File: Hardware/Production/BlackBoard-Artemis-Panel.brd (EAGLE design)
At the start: 167.6 x 120.9 mm, 522 parts, among them IC1 LM1117, IC2 LM1117, IC3 LM1117, IC4 LM1117, J10 CORTEX_DEBUG, J13 POWER_JACKTOE, J15 USB-C, J16 CORTEX_DEBUG, J19 POWER_JACKTOE, J2 CORTEX_DEBUG, J21 USB-C, J22 CORTEX_DEBUG, J3 POWER_JACKTOE, J5 USB-C, J6 POWER_JACKTOE, J9 USB-C, Q1 1.1A/60V/600mΩ, Q2 1.1A/60V/600mΩ, Q3 1.1A/60V/600mΩ, Q4 1.1A/60V/600mΩ, U1 AP2112-3.3V, U10 AP2112-3.3V, U11 CH340C, U12 ARTEMIS_MODULESMD, U2 CH340C, U3 AP2112-3.3V, U4 ARTEMIS_MODULESMD, U5 CH340C, U6 ARTEMIS_MODULESMD, U7 AP2112-3.3V, U8 CH340C, U9 ARTEMIS_MODULESMD, Y1 32.768kHz, Y2 32.768kHz, Y3 32.768kHz, Y4 32.768kHz

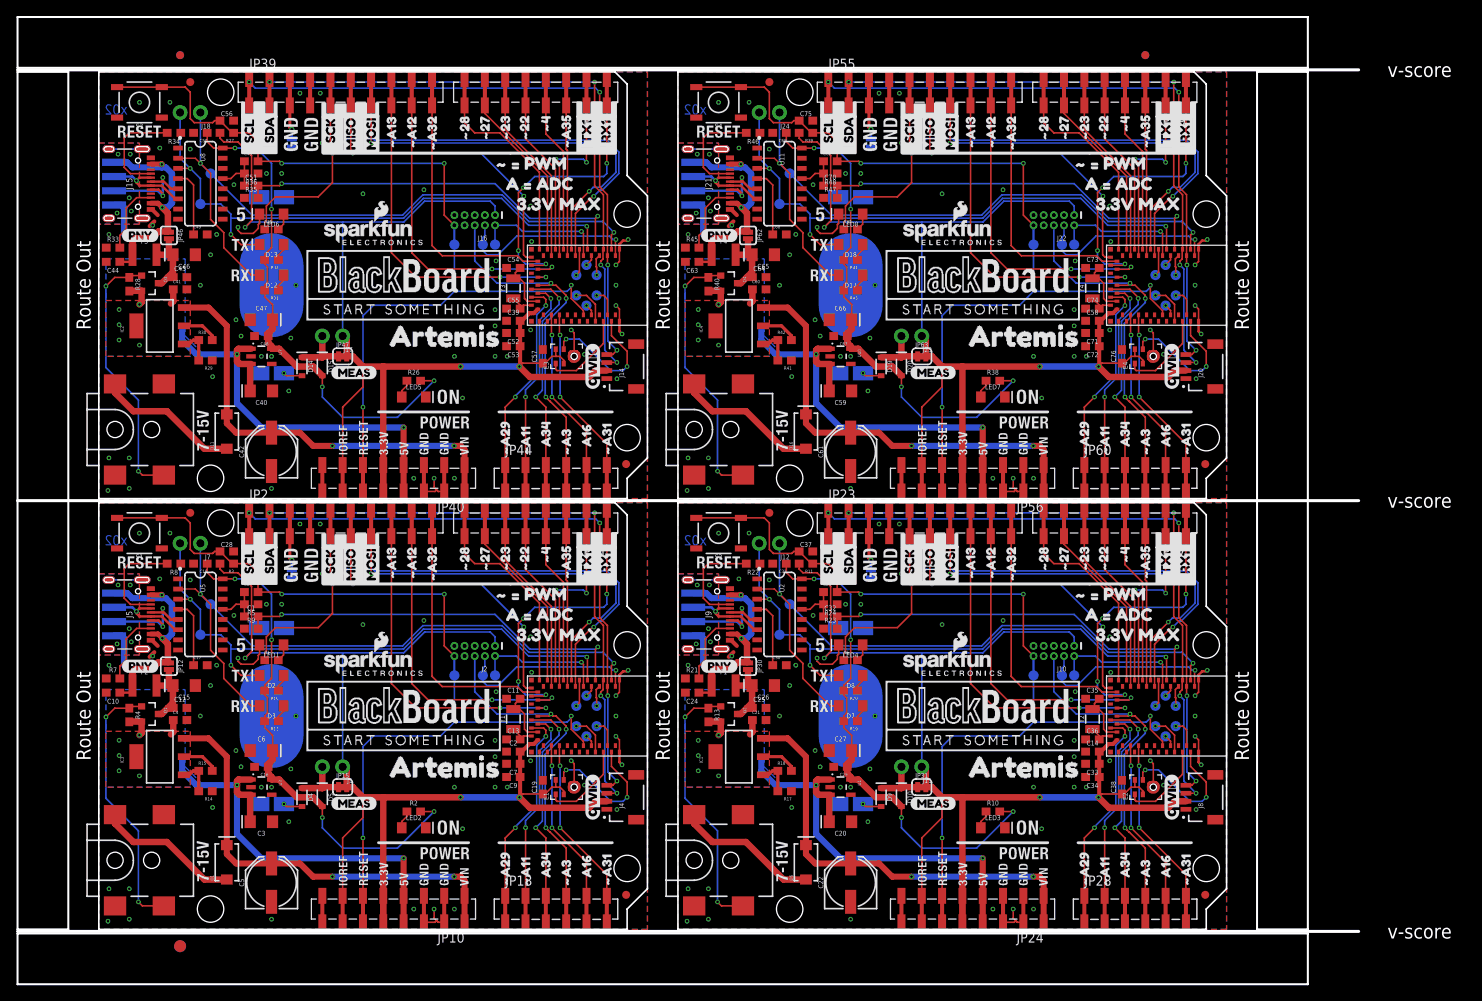
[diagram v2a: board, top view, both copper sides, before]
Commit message: Adding ignore. Adding production panel.
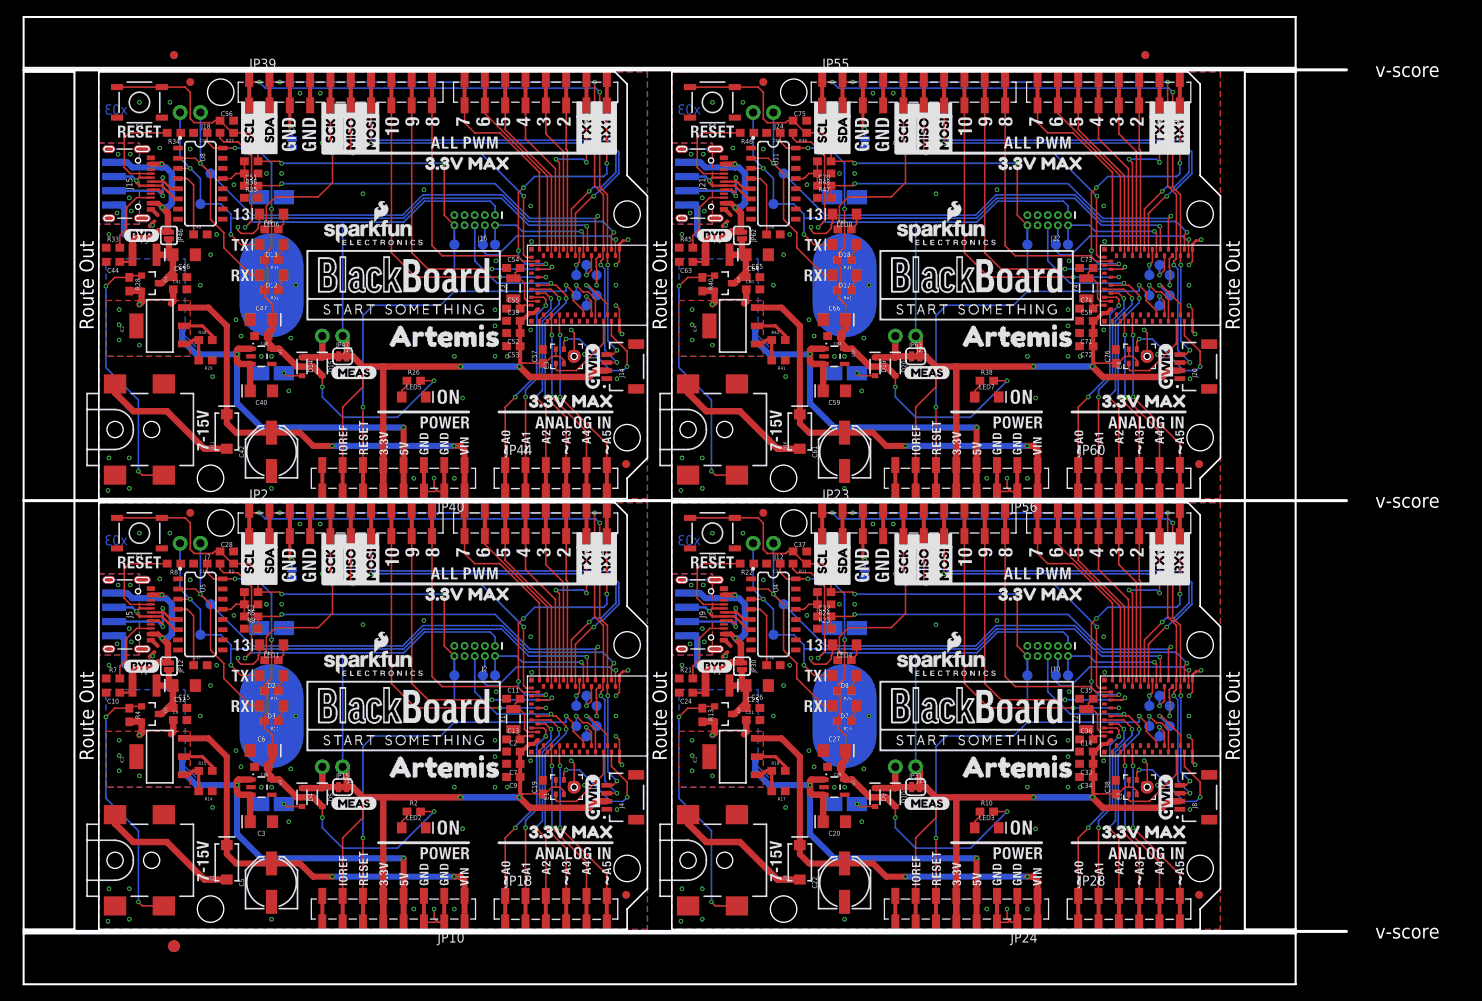
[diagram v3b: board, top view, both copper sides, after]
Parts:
- removed U$125, U$172: (no value), buzzard_labels (1):#425
- removed U$126, U$173: (no value), buzzard_labels (1):#434
- removed U$127, U$174: (no value), buzzard_labels (1):80
- removed U$128, U$175: (no value), buzzard_labels (1):91
- removed U$129, U$176: (no value), buzzard_labels (1):102
- removed U$130, U$177: (no value), buzzard_labels (1):383
- removed U$131, U$178: (no value), buzzard_labels (2):#_#_PWM7
- removed U$132, U$179: (no value), buzzard_labels (2):3#3V_MAX2
- removed U$133, U$180: (no value), buzzard_labels (2):A_#_ADC6
- removed U$134, U$181: (no value), buzzard_labels (2):MEAS3
- removed U$135, U$182: (no value), buzzard_labels (2):RX11
- removed U$136, U$183: (no value), buzzard_labels (2):TX10
- removed U$137, U$184: (no value), buzzard_labels (3):RX01
- removed U$138, U$185: (no value), buzzard_labels (3):TX00
- removed U$139, U$186: (no value), buzzard_labels (5):AREF2
- removed U$140, U$187: (no value), buzzard_labels (6):SCL1
- removed U$141, U$188: (no value), buzzard_labels (6):SDA0
- removed U$142: OSHW-LOGOS, SparkFun-Aesthetics:OSHW-LOGO-S
- removed U$143, U$144: (no value), blackboardlogo:BLACKBOARDLOGO#PNG
- removed U$145: (no value), madeinusa:MADEINUSA#PNG
- removed U$146: (no value), Labels:QWIIC_COPYRIGHT_SMALL
- removed U$147: (no value), buzzard_labels (13):G1
- removed U$148: (no value), buzzard_labels (13):V0
- removed U$149: (no value), buzzard_labels (14):D#3
- removed U$150: (no value), buzzard_labels (14):D#4
- removed U$151: (no value), buzzard_labels:PNY0
- removed U$152, U$153: (no value), buzzard_labels (3):ARTEMIS0
- removed U$154: (no value), buzzard_labels:A160
- removed U$155: (no value), buzzard_labels (1):#48
- removed U$156: (no value), buzzard_labels (1):#229
- removed U$157: (no value), buzzard_labels (1):#2310
- removed U$158: (no value), buzzard_labels (1):#2711
- removed U$159: (no value), buzzard_labels (1):#2812
- removed U$160: (no value), buzzard_labels (1):#A31
- removed U$161: (no value), buzzard_labels (1):#A113
- removed U$162: (no value), buzzard_labels (1):#A294
- removed U$163: (no value), buzzard_labels (1):#A310
- removed U$164: (no value), buzzard_labels (1):#A357
- removed U$165: (no value), buzzard_labels (1):#A1214
- removed U$166: (no value), buzzard_labels (1):#A1315
- removed U$167: (no value), buzzard_labels (1):#A3213
- removed U$168: (no value), buzzard_labels (1):A342
- removed U$169: (no value), buzzard_labels (8):MISO8
- removed U$170: (no value), buzzard_labels (8):MOSI7
- removed U$171: (no value), buzzard_labels (8):SCK9
- U$100: device buzzard_labels (13):G1 -> buzzard_labels (13):V0
- U$101: device buzzard_labels (13):V0 -> buzzard_labels (14):D#3
- U$102: device buzzard_labels (14):D#3 -> buzzard_labels (14):D#4
- U$103: device buzzard_labels (14):D#4 -> buzzard_labels (3):ARTEMIS0
- U$104: device buzzard_labels:PNY0 -> buzzard_labels (3):ARTEMIS0
- U$105: device buzzard_labels (3):ARTEMIS0 -> buzzard_labels (8):MISO8
- U$106: device buzzard_labels (3):ARTEMIS0 -> buzzard_labels (8):MOSI7
- U$107: device buzzard_labels:A160 -> buzzard_labels (8):SCK9
- U$108: device buzzard_labels (1):#48 -> buzzard_labels (2):3#3V_MAX2
- U$109: device buzzard_labels (1):#229 -> buzzard_labels (2):MEAS3
- U$110: device buzzard_labels (1):#2310 -> buzzard_labels (2):RX11
- U$111: device buzzard_labels (1):#2711 -> buzzard_labels (2):TX10
- U$112: device buzzard_labels (1):#2812 -> buzzard_labels (3):RX01
- U$113: device buzzard_labels (1):#A31 -> buzzard_labels (3):TX00
- U$114: device buzzard_labels (1):#A113 -> buzzard_labels (5):AREF2
- U$115: device buzzard_labels (1):#A294 -> buzzard_labels (6):SCL1
- U$116: device buzzard_labels (1):#A310 -> buzzard_labels (6):SDA0
- U$117: device buzzard_labels (1):#A357 -> buzzard_labels (13):BYP0
- U$118: device buzzard_labels (1):#A1214 -> buzzard_labels (2):3#3V_MAX2
- U$119: device buzzard_labels (1):#A1315 -> buzzard_labels (2):#284
- U$120: device buzzard_labels (1):#A3213 -> buzzard_labels (2):#295
- U$121: device buzzard_labels (1):A342 -> buzzard_labels (2):240
- U$122: device buzzard_labels (8):MISO8 -> buzzard_labels (2):251
- U$123: device buzzard_labels (8):MOSI7 -> buzzard_labels (2):262
- U$124: device buzzard_labels (8):SCK9 -> buzzard_labels (2):273
- U$13: device buzzard_labels:PNY0 -> buzzard_labels (2):3#3V_MAX2
- U$17: device buzzard_labels:A160 -> buzzard_labels (2):#284
- U$19: device buzzard_labels (1):#48 -> buzzard_labels (2):#295
- U$21: device buzzard_labels (1):#229 -> buzzard_labels (2):240
- U$23: device Labels:QWIIC_COPYRIGHT_SMALL -> buzzard_labels (2):251
- U$24: device buzzard_labels (13):G1 -> buzzard_labels (2):262
- U$25: device buzzard_labels (1):#2310 -> buzzard_labels (2):273
- U$26: device buzzard_labels (1):#2711 -> Labels:QWIIC_COPYRIGHT_SMALL
- U$27: device buzzard_labels (1):#2812 -> buzzard_labels (13):G1
- U$28: device buzzard_labels (1):#A31 -> buzzard_labels (13):V0
- U$29: device buzzard_labels (1):#A113 -> buzzard_labels (14):D#3
- U$30: device buzzard_labels (1):#A294 -> buzzard_labels (14):D#4
- U$31: device buzzard_labels (1):#A310 -> buzzard_labels (3):ARTEMIS0
- U$32: device buzzard_labels (13):V0 -> buzzard_labels (3):ARTEMIS0
- U$33: device buzzard_labels (1):#A357 -> buzzard_labels (8):MISO8
- U$34: device buzzard_labels (1):#A1214 -> buzzard_labels (8):MOSI7
- U$35: device buzzard_labels (1):#A1315 -> buzzard_labels (8):SCK9
- U$36: device buzzard_labels (1):#A3213 -> buzzard_labels (2):3#3V_MAX2
- U$37: device buzzard_labels (14):D#3 -> buzzard_labels (2):MEAS3
- U$38: device buzzard_labels (1):A342 -> buzzard_labels (2):RX11
- U$39: device buzzard_labels (14):D#4 -> buzzard_labels (2):TX10
- U$40: device buzzard_labels:PNY0 -> buzzard_labels (3):RX01
- U$41: device buzzard_labels (3):ARTEMIS0 -> buzzard_labels (3):TX00
- U$42: device buzzard_labels (3):ARTEMIS0 -> buzzard_labels (5):AREF2
- U$43: device buzzard_labels:A160 -> buzzard_labels (6):SCL1
- U$44: device buzzard_labels (1):#48 -> buzzard_labels (6):SDA0
- U$45: device buzzard_labels (1):#229 -> buzzard_labels (13):BYP0
- U$46: device buzzard_labels (1):#2310 -> buzzard_labels (2):3#3V_MAX2
- U$51: device buzzard_labels (1):#2711 -> buzzard_labels (2):#284
- U$52: device buzzard_labels (1):#2812 -> buzzard_labels (2):#295
- U$54: device buzzard_labels (1):#A31 -> buzzard_labels (2):240
- U$55: device buzzard_labels (1):#A113 -> buzzard_labels (2):251
- U$56: device buzzard_labels (1):#A294 -> buzzard_labels (2):262
- U$57: device buzzard_labels (1):#A310 -> buzzard_labels (2):273
- U$58: value (none) -> OSHW-LOGOS; device buzzard_labels (1):#A357 -> SparkFun-Aesthetics:OSHW-LOGO-S
- U$59: device buzzard_labels (1):#A1214 -> blackboardlogo:BLACKBOARDLOGO#PNG
- U$60: device buzzard_labels (1):#425 -> blackboardlogo:BLACKBOARDLOGO#PNG
- U$61: device buzzard_labels (1):#434 -> madeinusa:MADEINUSA#PNG
- U$62: device buzzard_labels (1):80 -> Labels:QWIIC_COPYRIGHT_SMALL
- U$63: device buzzard_labels (1):91 -> buzzard_labels (13):G1
- U$64: device buzzard_labels (1):102 -> buzzard_labels (13):V0
- U$65: device buzzard_labels (1):383 -> buzzard_labels (14):D#3
- U$66: device buzzard_labels (2):#_#_PWM7 -> buzzard_labels (14):D#4
- U$68: device buzzard_labels (1):#A1315 -> buzzard_labels (13):BYP0
- U$69: device buzzard_labels (2):A_#_ADC6 -> buzzard_labels (3):ARTEMIS0
- U$73: device buzzard_labels (1):#A3213 -> buzzard_labels (3):ARTEMIS0
- U$74: device buzzard_labels (1):A342 -> buzzard_labels (8):MISO8
- U$75: device buzzard_labels (8):MISO8 -> buzzard_labels (8):MOSI7
- U$76: device buzzard_labels (8):MOSI7 -> buzzard_labels (8):SCK9
- U$77: device buzzard_labels (8):SCK9 -> buzzard_labels (2):3#3V_MAX2
- U$78: device buzzard_labels (1):#425 -> buzzard_labels (2):MEAS3
- U$79: device buzzard_labels (1):#434 -> buzzard_labels (2):RX11
- U$80: device buzzard_labels (1):80 -> buzzard_labels (2):TX10
- U$81: device buzzard_labels (1):91 -> buzzard_labels (3):RX01
- U$82: device buzzard_labels (1):102 -> buzzard_labels (3):TX00
- U$83: device buzzard_labels (1):383 -> buzzard_labels (5):AREF2
- U$84: device buzzard_labels (2):#_#_PWM7 -> buzzard_labels (6):SCL1
- U$85: device buzzard_labels (2):3#3V_MAX2 -> buzzard_labels (6):SDA0
- U$86: device buzzard_labels (2):A_#_ADC6 -> buzzard_labels (13):BYP0
- U$87: device buzzard_labels (2):MEAS3 -> buzzard_labels (2):3#3V_MAX2
- U$88: device buzzard_labels (2):RX11 -> buzzard_labels (2):#284
- U$89: device buzzard_labels (2):TX10 -> buzzard_labels (2):#295
- U$90: device buzzard_labels (3):RX01 -> buzzard_labels (2):240
- U$91: device buzzard_labels (3):TX00 -> buzzard_labels (2):251
- U$92: device buzzard_labels (5):AREF2 -> buzzard_labels (2):262
- U$93: device buzzard_labels (6):SCL1 -> buzzard_labels (2):273
- U$94: value (none) -> OSHW-LOGOS; device buzzard_labels (6):SDA0 -> SparkFun-Aesthetics:OSHW-LOGO-S
- U$95: value OSHW-LOGOS -> (none); device SparkFun-Aesthetics:OSHW-LOGO-S -> blackboardlogo:BLACKBOARDLOGO#PNG
- U$97: device blackboardlogo:BLACKBOARDLOGO#PNG -> madeinusa:MADEINUSA#PNG
- U$98: device madeinusa:MADEINUSA#PNG -> Labels:QWIIC_COPYRIGHT_SMALL
- U$99: device Labels:QWIIC_COPYRIGHT_SMALL -> buzzard_labels (13):G1
- U1: value AP2112-3.3V -> ARTEMIS_MODULESMD; device SparkFun-PowerIC:SOT23-5 -> Testing:ARTEMIS_FP
- U2: value CH340C -> AP2112-3.3V; device SparkFun-IC-Comms:SO016 -> SparkFun-PowerIC:SOT23-5
- U4: value ARTEMIS_MODULESMD -> CH340C; device Testing:ARTEMIS_FP -> SparkFun-IC-Comms:SO016
- moved U$81 142.6 mm to (12.7, 96.3), turned to 90 degrees
- moved U$58 142.6 mm to (2.54, 105.2), flipped to the bottom, turned to 0 degrees
- moved U$82 140.8 mm to (10.2, 96.3), turned to 90 degrees
- moved U$83 134.8 mm to (26.9, 100.6)
- moved U$74 132.8 mm to (31.5, 96.4)
- moved U$86 128.0 mm to (3.05, 86.7)
- moved U$104 124.1 mm to (126.7, 91.9), flipped to the bottom
- moved U$85 118.4 mm to (21.3, 97.3), turned to 90 degrees
- moved U$84 115.9 mm to (18.8, 97.3), turned to 90 degrees
- moved U$78 111.4 mm to (29.0, 69.6), flipped to the top
- moved U$124 110.7 mm to (138.2, 79.2), flipped to the bottom, turned to 0 degrees
- moved U$95 110.0 mm to (109.7, 80.5), flipped to the top
- moved U$122 107.7 mm to (138.2, 81.8), flipped to the bottom, turned to 0 degrees
- moved U$68 106.4 mm to (3.05, 32.9), turned to 0 degrees
- moved U$79 104.0 mm to (63.4, 97.3), flipped to the top, turned to 90 degrees
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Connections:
- net AD1 renamed D20/A1
- net AD2 renamed D18/A1
- net AD3 renamed D20/A2
- net AD4 renamed D18/A3
- net AD5 renamed D20/A3
- net AD6 renamed D18/A4
- net D40/SDA1 renamed D14/SDA1
- net D40/SDA2 renamed D14/SDA2
- net D40/SDA3 renamed D14/SDA3
- net D7/MOSI1 renamed ~D11/MOSI1
- net D7/MOSI2 renamed ~D11/MOSI2
- net D7/MOSI3 renamed ~D11/MOSI3
- net ~AD1 renamed ~D21/A1
- net ~AD10 renamed ~D17/A3
- net ~AD14 renamed ~D2/A2
- net ~AD15 renamed ~D8/A2
- net ~AD16 renamed ~D9/A2
- net ~AD17 renamed ~D10/A2
- net ~AD18 renamed ~D21/A3
- net ~AD19 renamed ~D16/A3
- net ~AD2 renamed ~D16/A1
- net ~AD20 renamed ~D17/A4
- net ~AD21 renamed ~D2/A3
- net ~AD22 renamed ~D8/A3
- net ~AD23 renamed ~D9/A3
- net ~AD24 renamed ~D10/A3
- net ~AD3 renamed ~D17/A2
- net ~AD3/SWO1 renamed ~D19/A1
- net ~AD3/SWO2 renamed ~D19/A2
- net ~AD3/SWO3 renamed ~D19/A4
- net ~AD4 renamed ~D2/A1
- net ~AD5 renamed ~D8/A1
- net ~AD6 renamed ~D9/A1
- net ~AD7 renamed ~D10/A1
- net ~AD8 renamed ~D21/A2
- net ~AD9 renamed ~D16/A2
- net ~D24/TXO-2 renamed ~D1/TXO-2
- net ~D24/TXO-3 renamed ~D1/TXO-3
- net ~D24/TXO-4 renamed ~D1/TXO-4
- net ~D25/RXI-2 renamed ~D0/RXI-2
- net ~D25/RXI-3 renamed ~D0/RXI-3
- net ~D25/RXI-4 renamed ~D0/RXI-4
- net ~D39/SCL1 renamed ~D15/SCL1
- net ~D39/SCL2 renamed ~D15/SCL2
- net ~D39/SCL3 renamed ~D15/SCL3
- net ~D5/SCK1 renamed ~D13/SCK1
- net ~D5/SCK2 renamed ~D13/SCK2
- net ~D5/SCK3 renamed ~D13/SCK3
- net ~D6/MISO1 renamed ~D12/MISO1
- net ~D6/MISO2 renamed ~D12/MISO2
- net ~D6/MISO3 renamed ~D12/MISO3
- removed net AD16: JP13.5A, JP13.5B, U4.AD16
- removed net AD34: JP13.3A, JP13.3B, U4.AD34
- removed net D13: TP43.P$1, U12.D9
- removed net D14: TP44.P$1, U12.D10
- removed net D15: TP41.P$1, U12.D38
- removed net D38: TP11.P$1, U4.D38
- removed net D40/SDA: J4.3, JP2.2A, JP2.2B, U4.D40
- removed net D7/MOSI: JP2.7A, JP2.7B, U4.D7
- removed net ~AD11: JP13.2A, JP13.2B, U4.~AD11
- removed net ~AD12: JP2.9A, JP2.9B, U4.~AD12
- removed net ~AD13: JP2.8A, JP2.8B, U4.~AD13
- removed net ~AD29: JP13.1A, JP13.1B, U4.~AD29
- removed net ~AD3/SWO: J2.6, JP13.4A, JP13.4B, U4.~AD33/SWO
- removed net ~AD31: JP13.6A, JP13.6B, U4.~AD31
- removed net ~AD32: JP2.10A, JP2.10B, U4.~AD32
- removed net ~AD35: JP11.3A, JP11.3B, U4.~AD35
- removed net ~D24/TXO-1: JP11.2A, JP11.2B, U4.~D24
- removed net ~D25/RXI-1: JP11.1A, JP11.1B, U4.~D25
- removed net ~D27: JP11.7A, JP11.7B, U4.~D27
- removed net ~D39/SCL: J4.4, JP2.1A, JP2.1B, U4.~D39
- removed net ~D42: TP9.P$1, U4.~D42
- removed net ~D43: TP8.P$1, U4.~D43
- removed net ~D5/SCK: JP2.5A, JP2.5B, R1.1, U4.~D5
- removed net ~D6/MISO: JP2.6A, JP2.6B, U4.~D6
- new net D14/SDA: J4.3, JP2.2A, JP2.2B, U1.D40
- new net D18/A2: JP13.3A, JP13.3B, U1.AD34
- new net D20/A4: JP13.5A, JP13.5B, U1.AD16
- new net D24: TP12.P$1, U1.D8
- new net D25: TP13.P$1, U1.D9
- new net D26: TP14.P$1, U1.D10
- new net D27: TP11.P$1, U1.D38
- new net ~D0/RXI-1: JP11.1A, JP11.1B, U1.~D25
- new net ~D1/TXO-1: JP11.2A, JP11.2B, U1.~D24
- new net ~D10/A10: JP2.8A, JP2.8B, U1.~AD13
- new net ~D11/MOSI: JP2.7A, JP2.7B, U1.D7
- new net ~D12/MISO: JP2.6A, JP2.6B, U1.~D6
- new net ~D13/SCK: JP2.5A, JP2.5B, R1.1, U1.~D5
- new net ~D15/SCL: J4.4, JP2.1A, JP2.1B, U1.~D39
- new net ~D16/A0: JP13.1A, JP13.1B, U1.~AD29
- new net ~D17/A1: JP13.2A, JP13.2B, U1.~AD11
- new net ~D19/A3: J2.6, JP13.4A, JP13.4B, U1.~AD33/SWO
- new net ~D2/A6: JP11.3A, JP11.3B, U1.~AD35
- new net ~D21/A5: JP13.6A, JP13.6B, U1.~AD31
- new net ~D25: TP40.P$1, U12.~D42
- new net ~D26: TP39.P$1, U12.~D43
- new net ~D29: TP8.P$1, U1.~D43
- new net ~D8/A8: JP2.10A, JP2.10B, U1.~AD32
- new net ~D9/A9: JP2.9A, JP2.9B, U1.~AD12
- net !DTR1: now also U4.13; no longer U2.13
- net !RESET: now also U1.~RST; no longer U4.~RST
- net 3.3V1: now also U2.5, U4.16; no longer U1.5, U2.16
- net 5V1: now also U2.1, U2.3; no longer U1.1, U1.3
- net BOOT: now also U1.BOOT; no longer U4.BOOT
- net D+1: now also U4.5; no longer U2.5
- net D-1: now also U4.6; no longer U2.6
- net D10: now also TP43.P$1, U12.D9; no longer TP14.P$1, U4.D10
- net D11: now also TP44.P$1, U12.D10; no longer TP30.P$1, U9.D38
- net D12: now also TP41.P$1, U12.D38; no longer TP42.P$1, U12.D8
- net D8: now also TP30.P$1, U9.D38; no longer TP12.P$1, U4.D8
- net D9: now also TP42.P$1, U12.D8; no longer TP13.P$1, U4.D9
- net GND: now also U1.GND@1, U1.GND@22, U1.GND@38, U1.GND@39, U1.GND@47, U1.GND@59; no longer U4.GND@1, U4.GND@22, U4.GND@38, U4.GND@39, U4.GND@47, U4.GND@59
- net GND1: now also U2.2, U4.1; no longer U1.2, U2.1
- net N$17: now also U4.4; no longer U2.4
- net N$7: now also U1.XO; no longer U4.XO
- net N$8: now also U1.XI; no longer U4.XI
- net PDMCLK: now also U1.~D37; no longer U4.~D37
- net PDMDATA: now also U1.D36; no longer U4.D36
- net RXI-0: now also U1.RXI-0; no longer U4.RXI-0
- net RXI-1: now also U4.2; no longer U2.2
- net SWDCK: now also U1.SWDCK; no longer U4.SWDCK
- net SWDIO: now also U1.SWDIO; no longer U4.SWDIO
- net TXO-0: now also U1.TXO-0; no longer U4.TXO-0
- net TXO-1: now also U4.3; no longer U2.3
- net VDD: now also U1.VDD@36, U1.VDD@37; no longer U4.VDD@36, U4.VDD@37
- net ~D10: now also JP27.8A, JP27.8B, U6.~D28; no longer JP43.5A, JP43.5B, U9.~D22
- net ~D11: now also TP18.P$1, U6.~D42; no longer JP43.6A, JP43.6B, U9.~D23
- net ~D12: now also TP17.P$1, U6.~D43; no longer JP43.7A, JP43.7B, U9.~D27
- net ~D13: now also JP43.4A, JP43.4B, U9.~D4; no longer JP43.8A, JP43.8B, U9.~D28
- net ~D14: now also JP43.5A, JP43.5B, U9.~D22; no longer TP29.P$1, U9.~D42
- net ~D15: now also JP43.6A, JP43.6B, U9.~D23; no longer TP28.P$1, U9.~D43
- net ~D16: now also JP43.7A, JP43.7B, U9.~D27; no longer JP59.4A, JP59.4B, U12.~D4
- net ~D17: now also JP43.8A, JP43.8B, U9.~D28; no longer JP59.5A, JP59.5B, U12.~D22
- net ~D18: now also TP29.P$1, U9.~D42; no longer JP59.6A, JP59.6B, U12.~D23
- net ~D19: now also TP28.P$1, U9.~D43; no longer JP59.7A, JP59.7B, U12.~D27
- net ~D20: now also JP59.4A, JP59.4B, U12.~D4; no longer JP59.8A, JP59.8B, U12.~D28
- net ~D21: now also JP59.5A, JP59.5B, U12.~D22; no longer TP40.P$1, U12.~D42
- net ~D22: now also JP59.6A, JP59.6B, U12.~D23; no longer JP11.5A, JP11.5B, U4.~D22
- net ~D23: now also JP59.7A, JP59.7B, U12.~D27; no longer JP11.6A, JP11.6B, U4.~D23
- net ~D24: now also JP59.8A, JP59.8B, U12.~D28; no longer TP39.P$1, U12.~D43
- net ~D28: now also TP9.P$1, U1.~D42; no longer JP11.8A, JP11.8B, U4.~D28
- net ~D3: now also JP11.4A, JP11.4B, U1.~D4; no longer JP27.6A, JP27.6B, U6.~D23
- net ~D4: now also JP11.5A, JP11.5B, U1.~D22; no longer JP11.4A, JP11.4B, U4.~D4
- net ~D5: now also JP11.6A, JP11.6B, U1.~D23; no longer JP27.7A, JP27.7B, U6.~D27
- net ~D6: now also JP11.7A, JP11.7B, U1.~D27; no longer JP27.8A, JP27.8B, U6.~D28
- net ~D7: now also JP11.8A, JP11.8B, U1.~D28; no longer TP18.P$1, U6.~D42
- net ~D8: now also JP27.6A, JP27.6B, U6.~D23; no longer TP17.P$1, U6.~D43
- net ~D9: now also JP27.7A, JP27.7B, U6.~D27; no longer JP43.4A, JP43.4B, U9.~D4
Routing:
- net ~D15/SCL: track 0.00 -> 82.4 mm, vias 0 -> 4
- net ~D39/SCL: track 82.3 -> 0.00 mm, vias 4 -> 0
- net D14/SDA: track 0.00 -> 81.8 mm, vias 0 -> 4
- net D40/SDA: track 81.7 -> 0.00 mm, vias 4 -> 0
- net ~D5/SCK: track 78.2 -> 0.00 mm, vias 2 -> 0
- net ~D13/SCK: track 0.00 -> 78.2 mm, vias 0 -> 2
- net ~D11/MOSI: track 0.00 -> 54.0 mm, vias 0 -> 2
- net D7/MOSI: track 54.0 -> 0.00 mm, vias 2 -> 0
- net ~D19/A3: track 0.00 -> 46.1 mm, vias 0 -> 3
- net ~AD3/SWO: track 46.1 -> 0.00 mm, vias 3 -> 0
- net ~D10/A10: track 0.00 -> 43.3 mm, vias 0 -> 2
- net ~AD13: track 43.3 -> 0.00 mm, vias 2 -> 0
- net ~D9/A9: track 0.00 -> 42.1 mm, vias 0 -> 2
- net ~AD12: track 42.1 -> 0.00 mm, vias 2 -> 0
- net ~D6/MISO: track 41.4 -> 0.00 mm, vias 2 -> 0
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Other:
- board size 167.6 x 120.9 mm -> 165.4 x 120.9 mm
- board text added: "x03"
- board text removed: "x02"
